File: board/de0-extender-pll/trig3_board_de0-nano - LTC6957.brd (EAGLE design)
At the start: 160 x 75 mm, 94 parts, among them IC1 FT230XQ, J12 4p-2.54, J13 BU-SMB-V, J17 2p-2.54, J23 2p-2.54, J24 2p-2.54, J32 2p-2.54, J34 2p-2.54, J38 2p-2.54, J42 2p-2.54, J43 2p-2.54, J7 4p-2.54, K15_P BU-SMB-V, K16N BU-SMB-V, P11 BU-SMB-V, P15 BU-SMB-V, P16_R15N BU-SMB-V, P9 BU-SMB-V, T13_B20N BU-SMB-V, U1 LTC6957IDD-2TRPBF

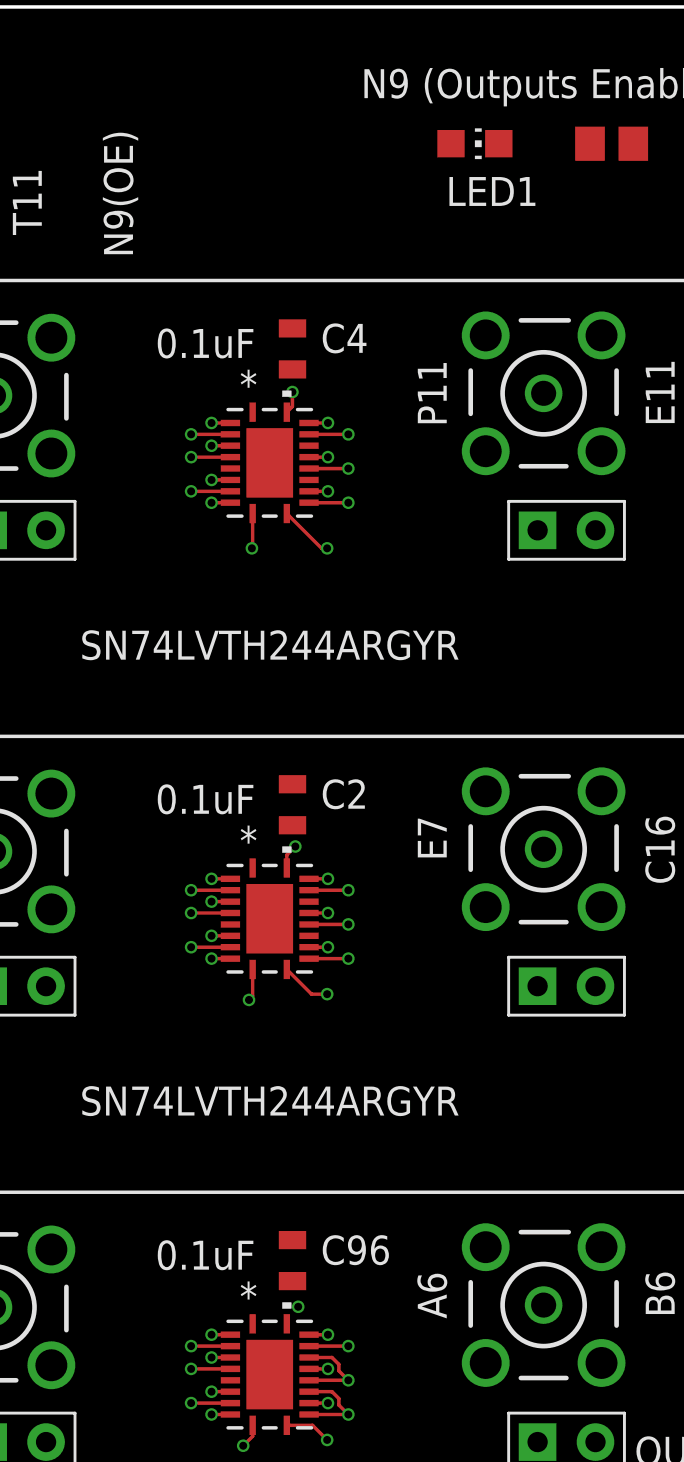
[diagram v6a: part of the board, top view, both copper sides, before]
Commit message: Update trig3_board_de0-nano - LTC6957.brd
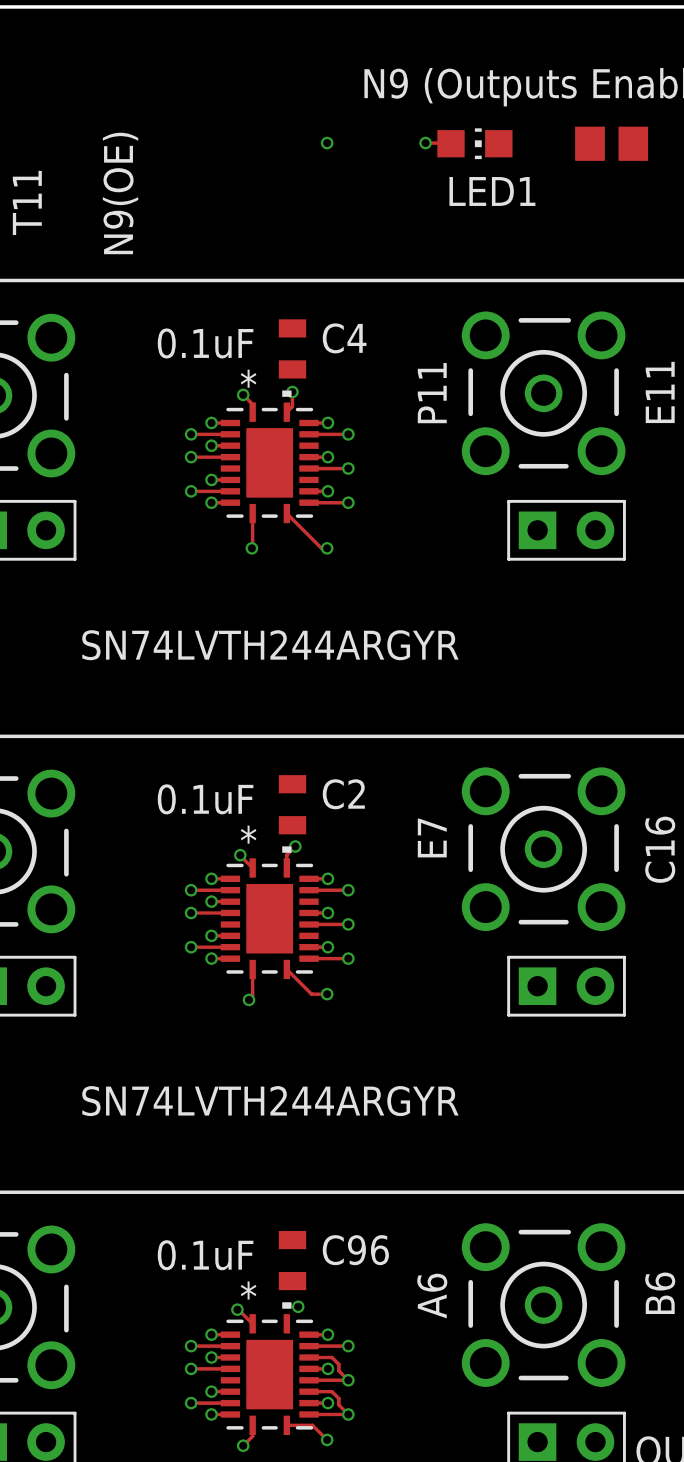
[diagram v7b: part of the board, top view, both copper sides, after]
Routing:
- net GPIO_114_N9: track 2.48 -> 77.1 mm, vias 3 -> 8
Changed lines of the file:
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@@
 <via x="88.553090625" y="52.75" extent="1-16" drill="0.35"/>
 <contactref element="VSLUE5" pad="19"/>
-<wire x1="88.553090625" y1="92.75" x2="93.95" y2="105" width="0" layer="19" extent="1-1"/>
-<wire x1="85.25" y1="93.225" x2="87.725" y2="92.75" width="0" layer="19" extent="1-1"/>
-<wire x1="85.25" y1="73.225" x2="87.725" y2="92.75" width="0" layer="19" extent="1-1"/>
-<wire x1="87.725" y1="72.75" x2="85.25" y2="73.225" width="0" layer="19" extent="1-1"/>
-<wire x1="85.25" y1="53.225" x2="87.725" y2="72.75" width="0" layer="19" extent="1-1"/>
-<wire x1="87.725" y1="52.75" x2="85.25" y2="53.225" width="0" layer="19" extent="1-1"/>
-<wire x1="52.31" y1="108.1" x2="85.25" y2="93.225" width="0" layer="19" extent="1-1"/>
+<wire x1="88.553090625" y1="52.75" x2="88.553090625" y2="66.386909375" width="0.1524" layer="15"/>
+<wire x1="88.553090625" y1="66.386909375" x2="87.757" y2="67.183" width="0.1524" layer="15"/>
+<wire x1="87.757" y1="67.183" x2="87.757" y2="71.953909375" width="0.1524" layer="15"/>
+<wire x1="87.757" y1="71.953909375" x2="88.553090625" y2="72.75" width="0.1524" layer="15"/>
+<wire x1="88.553090625" y1="72.75" x2="88.553090625" y2="86.325909375" width="0.1524" layer="15"/>
+<wire x1="88.553090625" y1="86.325909375" x2="87.757" y2="87.122" width="0.1524" layer="15"/>
+<wire x1="87.757" y1="87.122" x2="87.757" y2="91.953909375" width="0.1524" layer="15"/>
+<wire x1="87.757" y1="91.953909375" x2="88.553090625" y2="92.75" width="0.1524" layer="15"/>
+<wire x1="88.553090625" y1="92.75" x2="88.553090625" y2="104.994909375" width="0.1524" layer="15"/>
+<wire x1="88.553090625" y1="104.994909375" x2="88.519" y2="105.029" width="0.1524" layer="15"/>
+<via x="88.519" y="105.029" extent="1-16" drill="0.35"/>
+<wire x1="88.519" y1="105.029" x2="92.837" y2="105.029" width="0.1524" layer="2"/>
+<via x="92.837" y="105.029" extent="1-16" drill="0.35"/>
+<wire x1="92.837" y1="105.029" x2="93.921" y2="105.029" width="0.1524" layer="1"/>
+<wire x1="93.921" y1="105.029" x2="93.95" y2="105" width="0.1524" layer="1"/>
+<wire x1="88.553090625" y1="92.75" x2="86.066" y2="92.75" width="0.1524" layer="2"/>
+<wire x1="86.066" y1="92.75" x2="84.836" y2="93.98" width="0.1524" layer="2"/>
+<via x="84.836" y="93.98" extent="1-16" drill="0.35"/>
+<wire x1="84.836" y1="93.98" x2="85.25" y2="93.566" width="0.1524" layer="1"/>
+<wire x1="85.25" y1="93.566" x2="85.25" y2="93.225" width="0.1524" layer="1"/>
+<wire x1="85.25" y1="73.225" x2="84.709" y2="73.766" width="0.1524" layer="1"/>
+<wire x1="84.709" y1="73.766" x2="84.709" y2="73.787" width="0.1524" layer="1"/>
+<via x="84.709" y="73.787" extent="1-16" drill="0.35"/>
+<wire x1="84.709" y1="73.787" x2="85.746" y2="72.75" width="0.1524" layer="2"/>
+<wire x1="85.746" y1="72.75" x2="88.553090625" y2="72.75" width="0.1524" layer="2"/>
+<wire x1="85.25" y1="53.225" x2="84.627" y2="53.848" width="0.1524" layer="1"/>
+<wire x1="84.627" y1="53.848" x2="84.582" y2="53.848" width="0.1524" layer="1"/>
+<via x="84.582" y="53.848" extent="1-16" drill="0.35"/>
+<wire x1="84.582" y1="53.848" x2="85.68" y2="52.75" width="0.1524" layer="2"/>
+<wire x1="85.68" y1="52.75" x2="88.553090625" y2="52.75" width="0.1524" layer="2"/>
+<wire x1="84.836" y1="93.98" x2="52.31" y2="108.1" width="0" layer="19" extent="1-1"/>
 <wire x1="8.97" y1="79.03" x2="52.31" y2="108.1" width="0" layer="19" extent="1-1"/>
 </signal>

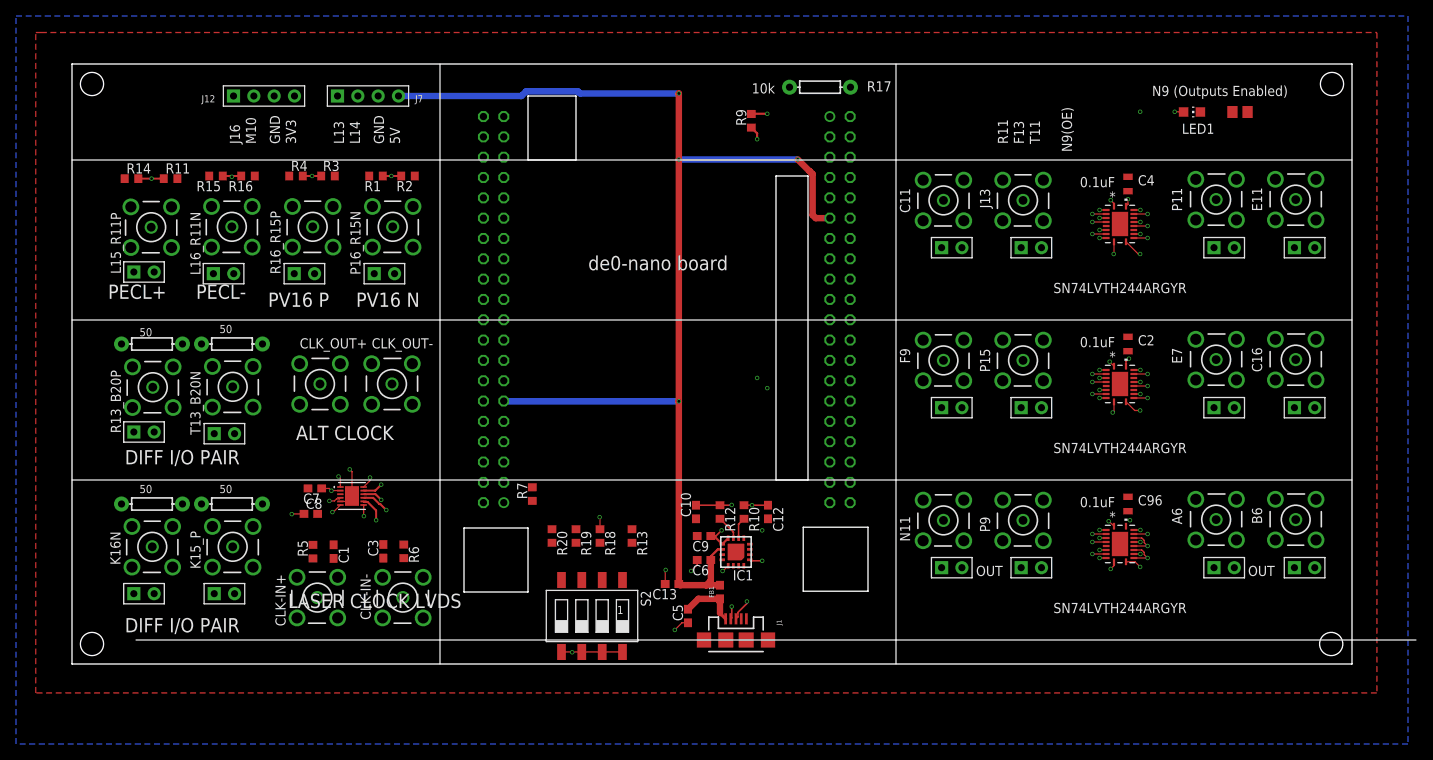
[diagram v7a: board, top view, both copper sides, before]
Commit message: routed - now needs aesthetic cleanup
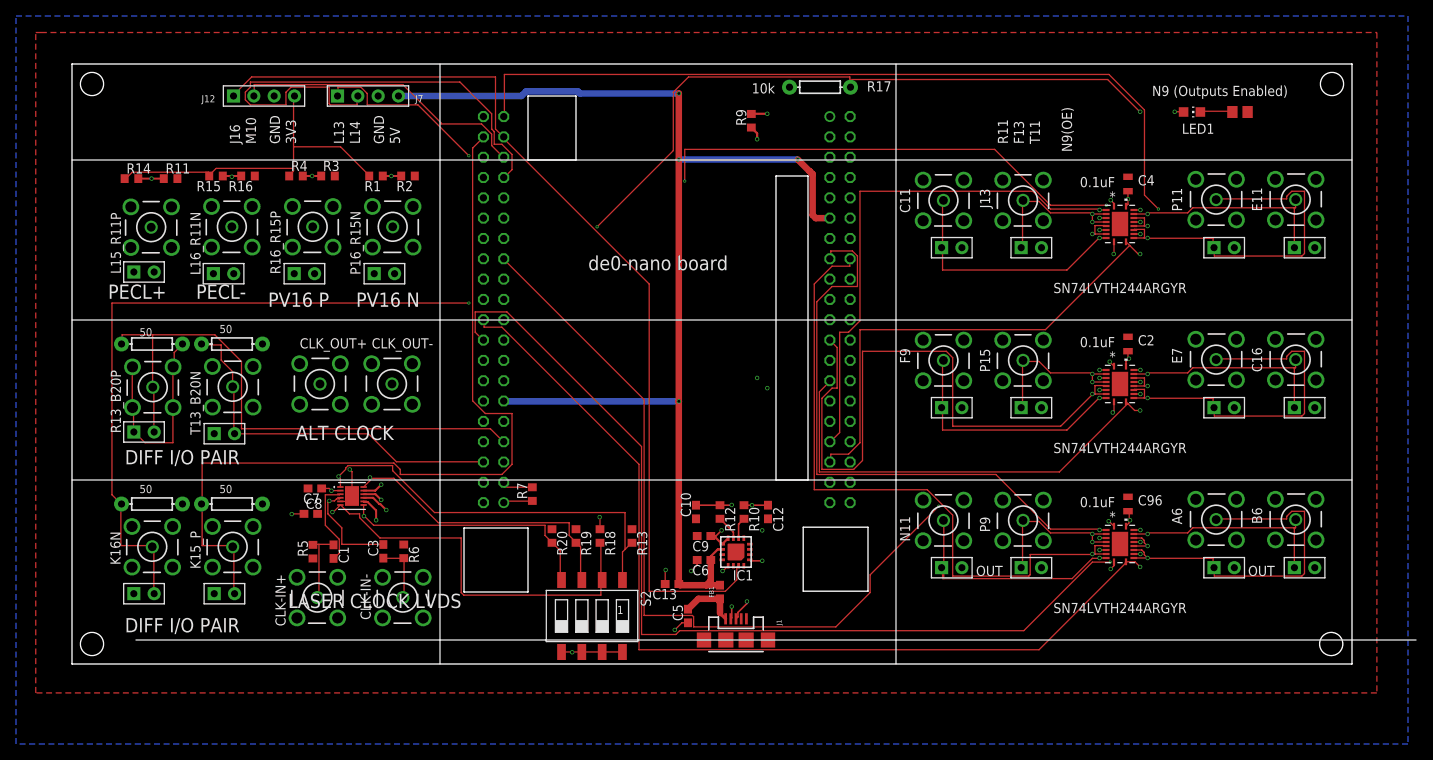
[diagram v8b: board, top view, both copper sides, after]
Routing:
- net GPIO_120_P15: track 1.72 -> 134.0 mm, vias 1 -> 2
- net GPIO_113_P9: track 4.03 -> 127.1 mm, vias 1 -> 2
- net GPIO_130_J16: track 0.00 -> 119.5 mm
- net GPIO_115_N11: track 4.49 -> 120.6 mm
- net GPIO_131_K15: track 0.00 -> 106.1 mm
- net GPIO_132_J13: track 1.72 -> 107.5 mm, vias 1 -> 2
- net GPIO_114_N9: track 77.1 -> 176.5 mm, vias 8 -> 9
- net GPIO_110_P11: track 1.72 -> 100.1 mm, vias 1 -> 3
- net GPIO_117_K16: track 0.00 -> 87.5 mm, vias 0 -> 1
- net GPIO_011_A6: track 1.72 -> 82.6 mm
- net GPIO_018_E7: track 1.72 -> 80.5 mm
- net GPIO_010_B6: track 1.66 -> 77.0 mm
- net GPIO_14_R13: track 0.00 -> 71.6 mm
- net GPIO_026_E11: track 1.66 -> 67.3 mm
- net GPIO_126_L14: track 0.00 -> 63.7 mm
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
